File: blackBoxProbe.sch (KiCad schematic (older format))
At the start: 34 parts, among them J1 USB-ID, U1 MCP1702-MB, U2 USBLC6-2, U3 STM32F103CBT

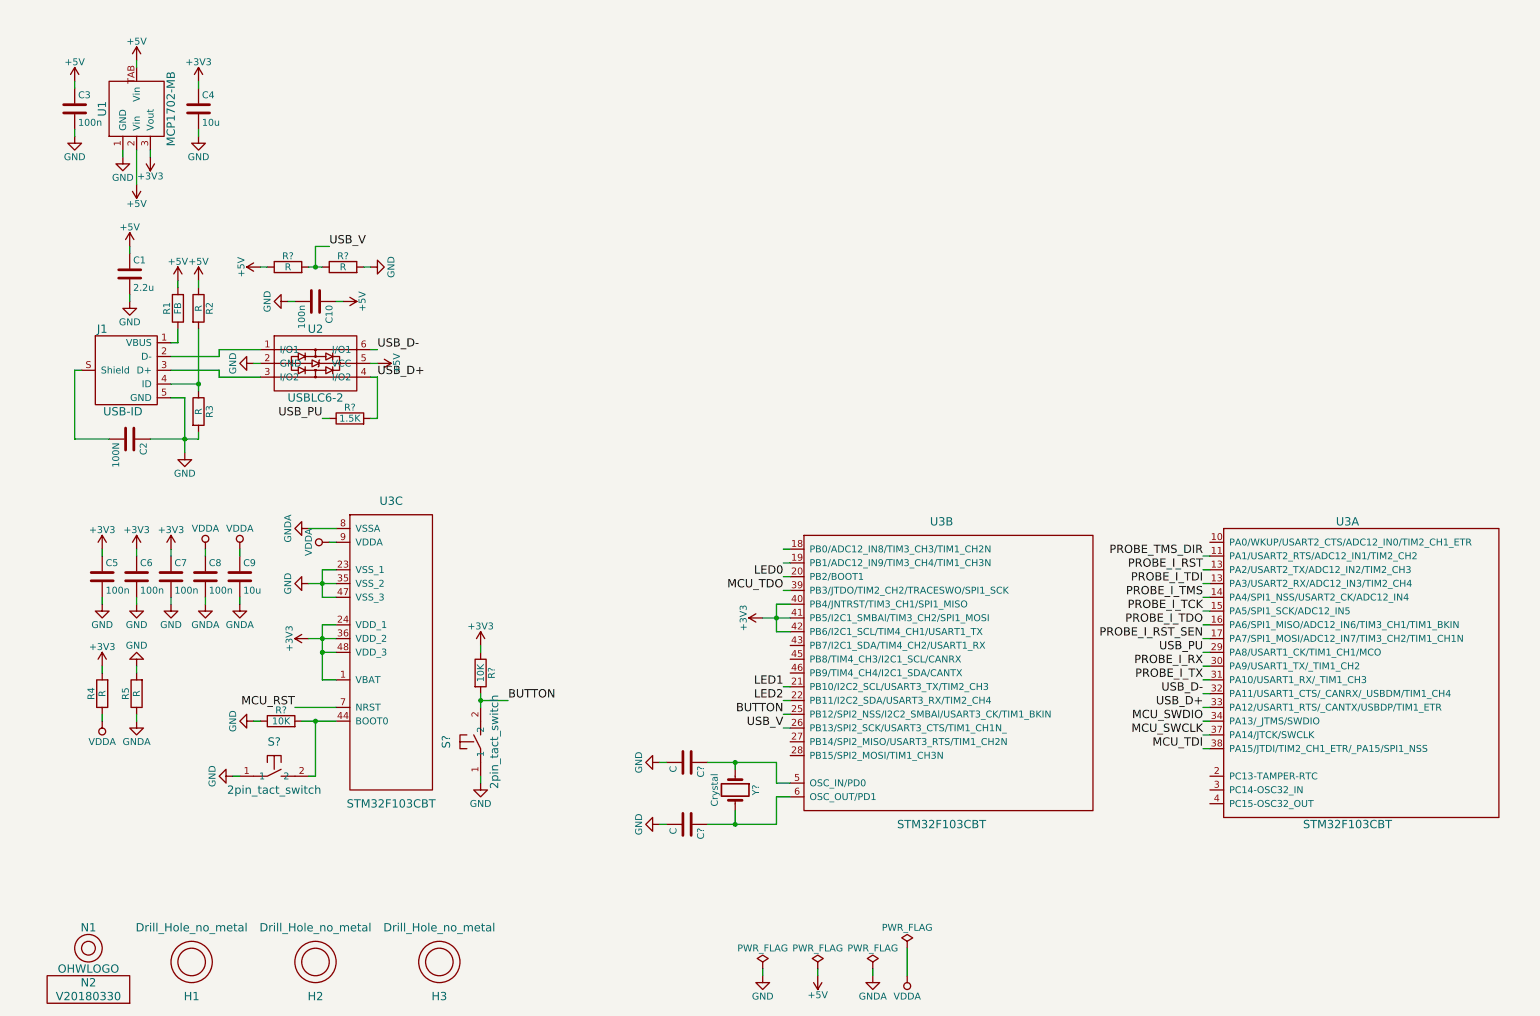
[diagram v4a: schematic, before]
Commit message: WIP: added JTAG/SWD interface bits, still reset sensing needs to be done
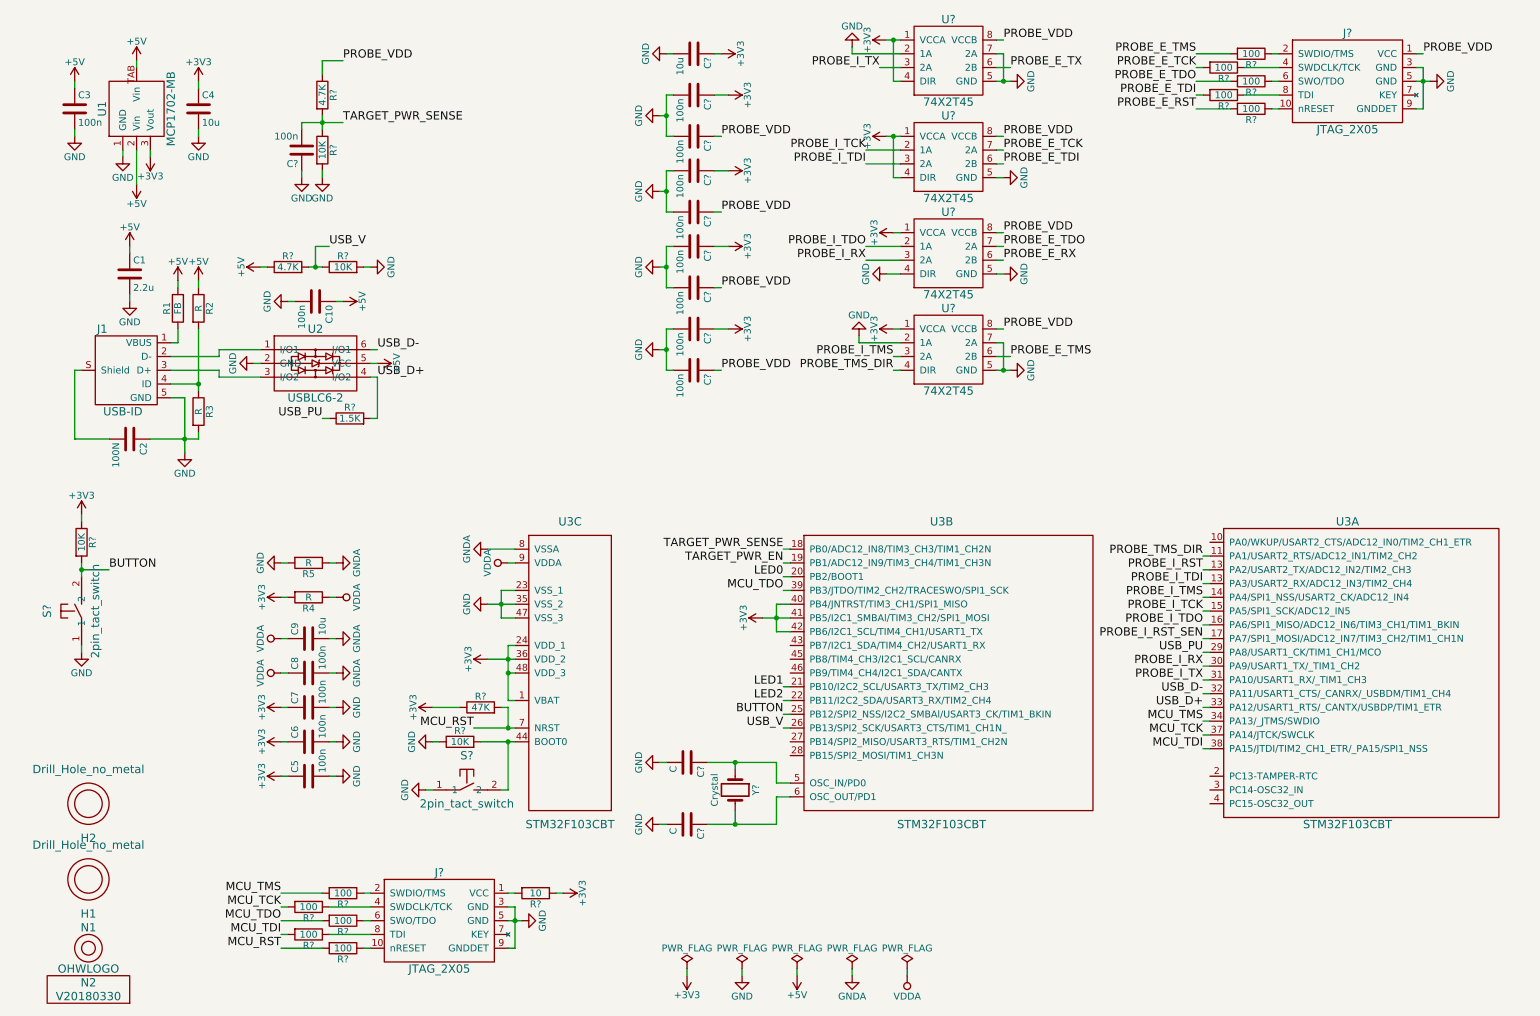
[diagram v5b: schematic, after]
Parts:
- removed H3: Drill_Hole_no_metal, SquantorPcbOutline:MountingHole_2.2mm_no_metal, symbol Drill_Hole_no_metal
- added C? (x9): 100n, SquantorRcl:C_0603, symbol C
- added C?: 10u, SquantorRcl:C_0805, symbol C
- added J? (x2): JTAG_2X05, symbol JTAG_2X05
- added R?: 10K, SquantorRcl:R_0603_hand, symbol R
- added R?: 4.7K, SquantorRcl:R_0603_hand, symbol R
- added R? (x10): 100, SquantorRcl:R_0603_hand, symbol R
- added R?: 10, SquantorRcl:R_0603_hand, symbol R
- added R?: 47K, SquantorRcl:R_0603_hand, symbol R
- added U? (x4): 74X2T45, symbol 74X2T45
- H1, H2: footprint SquantorPcbOutline:MountingHole_3.2mm_no_metal -> SquantorPcbOutline:MountingHole_2.5mm_no_metal
- R?: value R -> 4.7K
- R?: value R -> 10K
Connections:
- net +3V3: now also C?.1, C?.1, C?.1, C?.1, C?.1, R?.1, R?.1, U?.1 (VCCA), U?.1 (VCCA), U?.1 (VCCA), U?.1 (VCCA), U?.4 (DIR), U?.4 (DIR)
- net GND: now also C?.1, C?.2, C?.2, C?.2, C?.2, C?.2, C?.2, C?.2, C?.2, C?.2, J?.3 (GND), J?.3 (GND), J?.5 (GND), J?.5 (GND), J?.9 (GNDDET), J?.9 (GNDDET), R?.2, U?.2 (1A), U?.2 (1A), U?.4 (DIR), U?.5 (GND), U?.5 (GND), U?.5 (GND), U?.5 (GND), U?.7 (2A), U?.7 (2A)
- net MCU_RST: now also R?.2, R?.2
- net MCU_TDI: now also R?.2
- net MCU_TDO: now also R?.2
- net PROBE_I_RX: now also U?.3 (2A)
- net PROBE_I_TCK: now also U?.2 (1A)
- net PROBE_I_TDI: now also U?.3 (2A)
- net PROBE_I_TDO: now also U?.2 (1A)
- net PROBE_I_TMS: now also U?.3 (2A)
- net PROBE_I_TX: now also U?.3 (2A)
- net PROBE_TMS_DIR: now also U?.4 (DIR)
- net TARGET_PWR_SENSE: now reaches U3.18 (PB0/ADC12_IN8/TIM3_CH3/TIM1_CH2N)
- net TARGET_PWR_SENSE: now also C?.2, R?.1, R?.2
- net TARGET_PWR_EN: now reaches U3.19 (PB1/ADC12_IN9/TIM3_CH4/TIM1_CH3N)
- net MCU_SWCLK renamed MCU_TCK
- net MCU_TCK: now also R?.2
- net MCU_SWDIO renamed MCU_TMS
- net MCU_TMS: now also R?.2
- new net: J?.1 (VCC), R?.2
- new net: J?.10 (nRESET), R?.1 (x2)
- new net: J?.2 (SWDIO/TMS), R?.1 (x2)
- new net: J?.4 (SWDCLK/TCK), R?.1 (x2)
- new net: J?.6 (SWO/TDO), R?.1 (x2)
- new net: J?.8 (TDI), R?.1 (x2)
- new net PROBE_E_RST: R?.2
- new net PROBE_E_RX: U?.6 (2B)
- new net PROBE_E_TCK: R?.2, U?.7 (2A)
- new net PROBE_E_TDI: R?.2, U?.6 (2B)
- new net PROBE_E_TDO: R?.2, U?.7 (2A)
- new net PROBE_E_TMS: R?.2, U?.6 (2B)
- new net PROBE_E_TX: U?.6 (2B)
- new net PROBE_VDD: C?.1, C?.1, C?.1, C?.1, J?.1 (VCC), R?.1, U?.8 (VCCB), U?.8 (VCCB), U?.8 (VCCB), U?.8 (VCCB)
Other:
- moved on the sheet: C5, C6, C7, C8, C9, H1, H2, R4, R5, R?, S?, U3C

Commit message: DONE: Finished schematic WIP: review WIP: Assign components
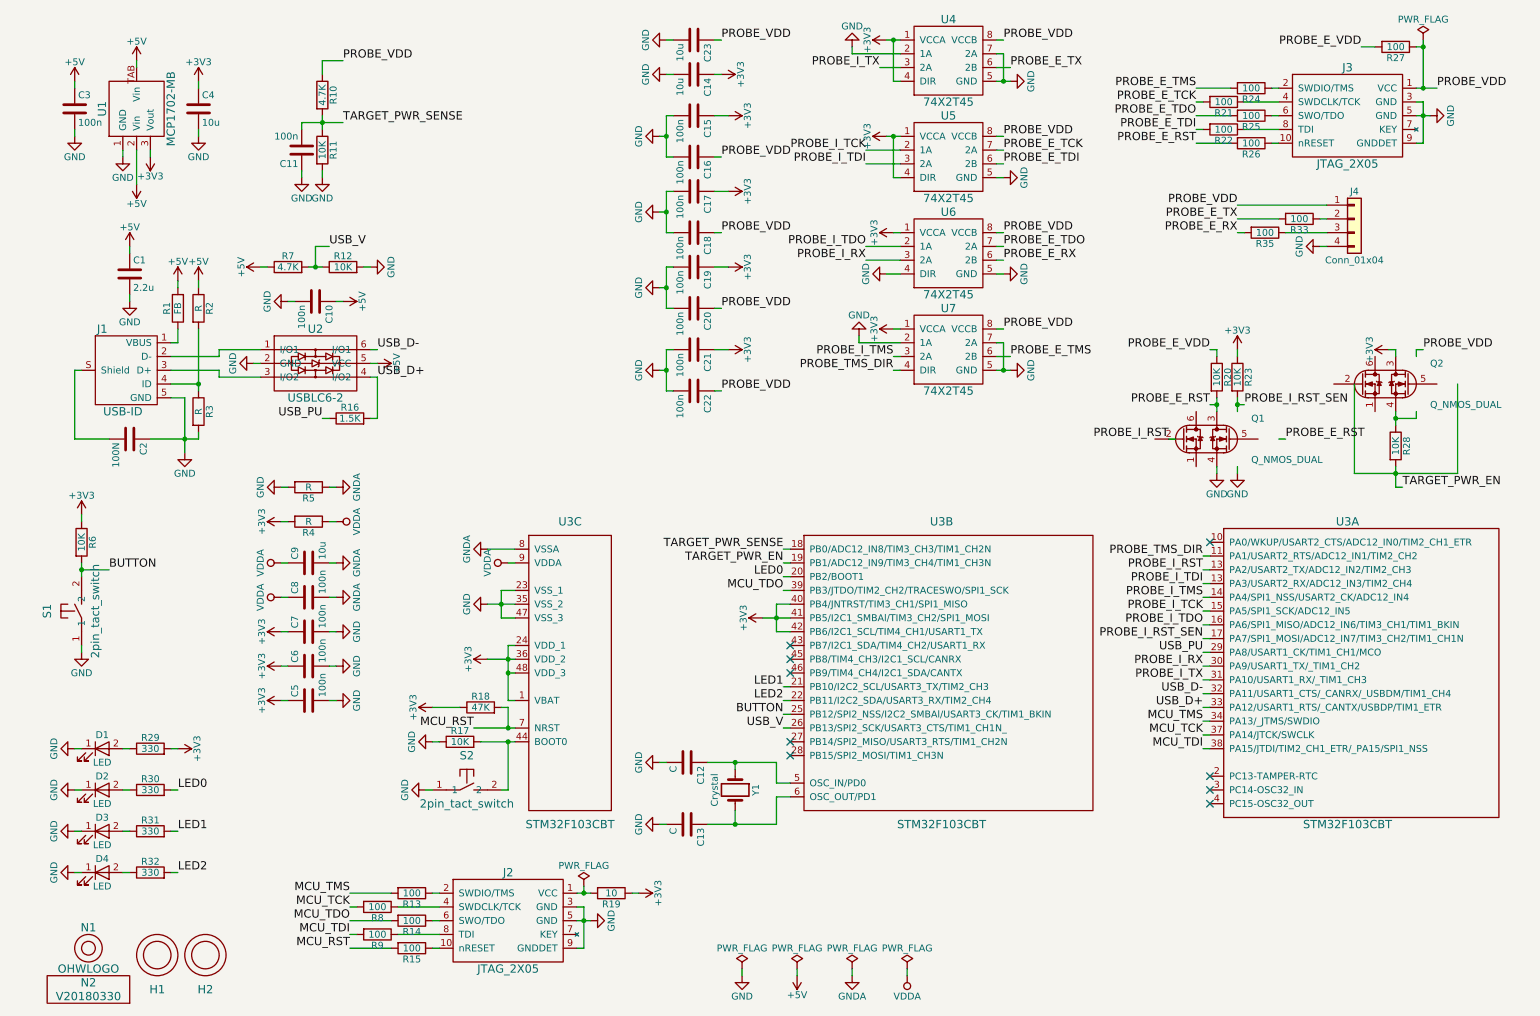
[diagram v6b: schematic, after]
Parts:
- added C23: 10u, SquantorRcl:C_0805, symbol C
- added D1, D2, D3, D4: LED, symbol LED
- added J4: Conn_01x04, symbol Conn_01x04
- added Q1, Q2: Q_NMOS_DUAL, symbol Q_NMOS_DUAL
- added R20, R23, R28: 10K, SquantorRcl:R_0603_hand, symbol R
- added R27, R33, R35: 100, SquantorRcl:R_0603_hand, symbol R
- added R29, R30, R31, R32: 330, SquantorRcl:R_0603_hand, symbol R
- C12, C13: renamed from C?; footprint (none) -> SquantorRcl:C_0603
- J2, J3: renamed from J?; footprint (none) -> SquantorConnectors:Header-0127-2X05-SMD
- U3: footprint SquantorIC:SOT313-2 -> (none)
- U4, U5, U6, U7: renamed from U?; footprint (none) -> SquantorIC:NXP_SOT765-1_HAND
- Y1: renamed from Y?; footprint (none) -> SquantorCrystal:SquantorCrystal-CRYSTAL_5.0X3.2
- gave numbers to parts that had none: 31
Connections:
- net +3V3: now also Q2.3 (D2), R23.1, R29.2
- net GND: now also C23.2, D1.1 (K), D2.1 (K), D3.1 (K), D4.1 (K), J4.4 (Pin_4), Q1.4 (S2)
- net LED0: now also R30.2
- net LED1: now also R31.2
- net LED2: now also R32.2
- net PROBE_E_RST: now also Q1.3 (D2), R20.2
- net PROBE_E_RX: now also R35.2
- net PROBE_E_TX: now also R33.2
- net PROBE_I_RST_SEN: now also R23.2
- net PROBE_VDD: now also C23.1, J4.1 (Pin_1), R27.1
- net TARGET_PWR_EN: now also R28.2
- new net: Q2.4 (S2), R28.1
- new net: D1.2 (A), R29.1
- new net: D2.2 (A), R30.1
- new net: D3.2 (A), R31.1
- new net: D4.2 (A), R32.1
- new net: J4.2 (Pin_2), R33.1
- new net: J4.3 (Pin_3), R35.1
- new net PROBE_E_VDD: R20.1, R27.2
- no-connect marks 0 -> 9
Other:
- moved on the sheet: C14, C15, C16, C17, C18, C19, C20, C21, C22, C5, C6, C7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

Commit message: FIX: fixed wrong schematic symbol for the switch, needs to be dual PMOS DONE: assigned all components a footprint
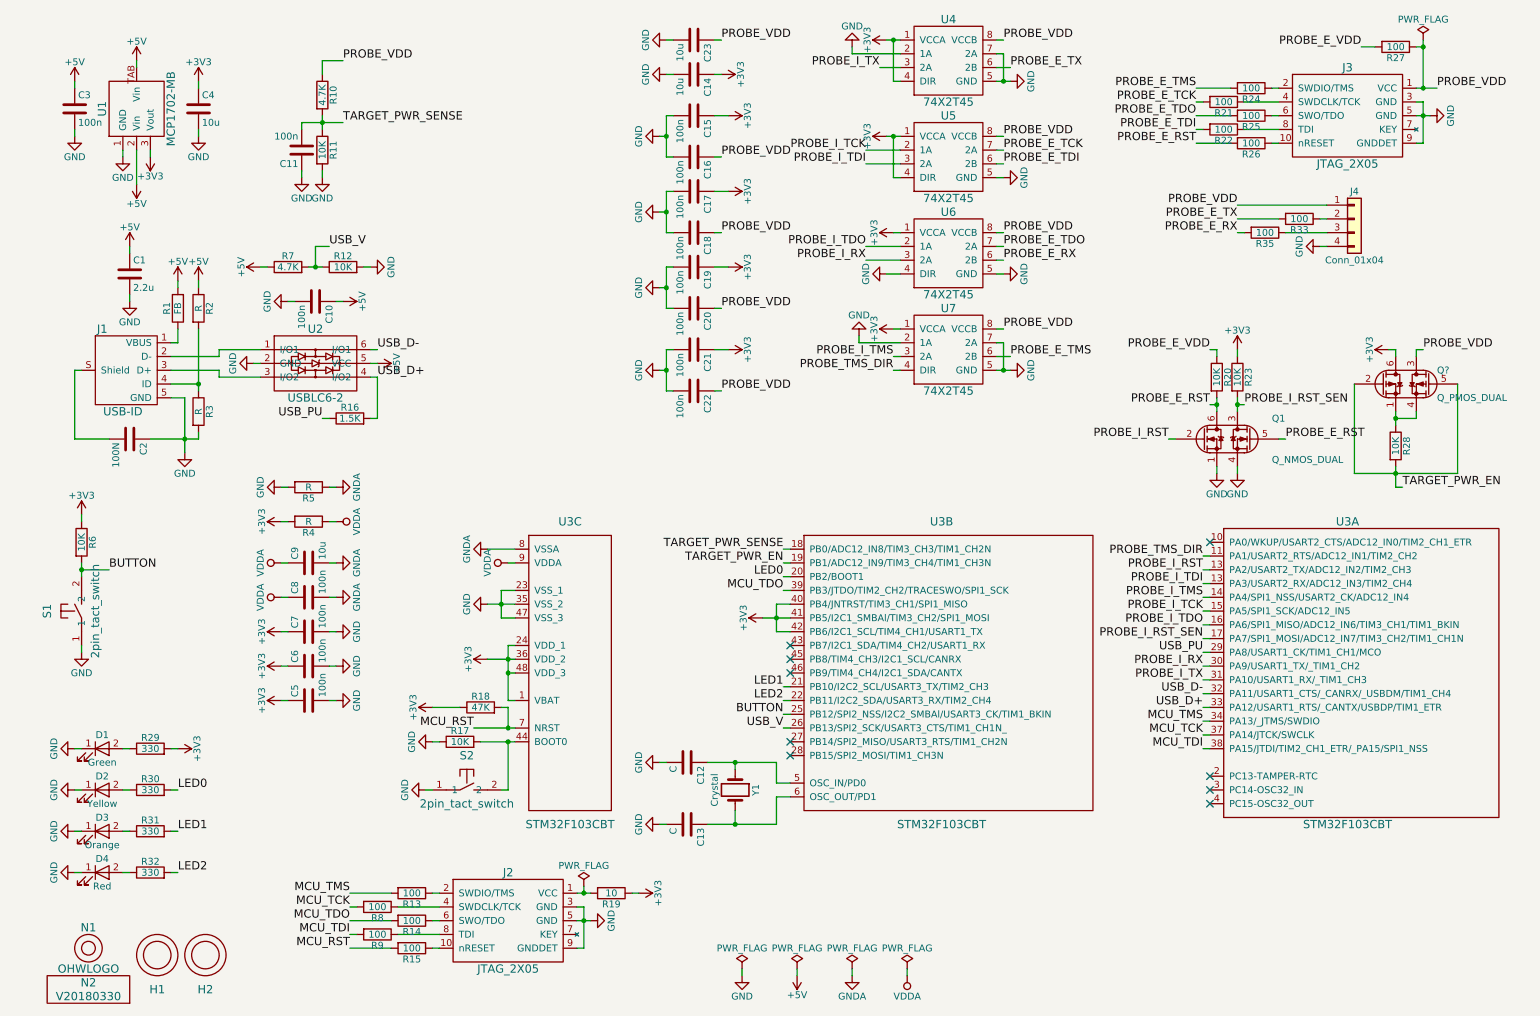
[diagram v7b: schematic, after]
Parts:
- removed Q2: Q_NMOS_DUAL, symbol Q_NMOS_DUAL
- added Q?: Q_PMOS_DUAL, TO_SOT_Packages_SMD:SOT-363_SC-70-6_Handsoldering, symbol Q_PMOS_DUAL
- D1: value LED -> Green; footprint (none) -> LEDs:LED_PLCC-2
- D2: value LED -> Yellow; footprint (none) -> LEDs:LED_PLCC-2
- D3: value LED -> Orange; footprint (none) -> LEDs:LED_PLCC-2
- D4: value LED -> Red; footprint (none) -> LEDs:LED_PLCC-2
- Q1: footprint (none) -> TO_SOT_Packages_SMD:SOT-363_SC-70-6_Handsoldering
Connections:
- net +3V3: now also Q?.6 (D1)
- net GND: now also Q1.1 (S1)
- net PROBE_E_RST: now also Q1.5 (G2), Q1.6 (D1); no longer Q1.3 (D2)
- net PROBE_I_RST: now also Q1.2 (G1)
- net PROBE_I_RST_SEN: now also Q1.3 (D2)
- net PROBE_VDD: now also Q?.3 (D2)
- net TARGET_PWR_EN: now also Q?.2 (G1), Q?.5 (G2)
- net at R28.1: now also Q?.1 (S1), Q?.4 (S2)
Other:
- moved on the sheet: Q1
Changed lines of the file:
@@
 L Q_NMOS_DUAL Q1
 U 1 1 5B245E45
-P 8950 3650
-F 0 "Q1" H 9300 3800 50  0000 L CNN
-F 1 "Q_NMOS_DUAL" H 9300 3500 50  0000 L CNN
-F 2 "" H 9150 3750 50  0001 C CNN
-F 3 "" H 8950 3650 50  0001 C CNN
-	1    8950 3650
+P 9100 3650
+F 0 "Q1" H 9450 3800 50  0000 L CNN
+F 1 "Q_NMOS_DUAL" H 9450 3500 50  0000 L CNN
+F 2 "TO_SOT_Packages_SMD:SOT-363_SC-70-6_Handsoldering" H 9300 3750 50  0001 C CNN
+F 3 "" H 9100 3650 50  0001 C CNN
+	1    9100 3650
 	1    0    0    -1
 $EndComp
@@
 Connection ~ 9200 3400
 $Comp
-L Q_NMOS_DUAL Q2
-U 1 1 5B24D809
-P 10250 3250
-F 0 "Q2" H 10600 3400 50  0000 L CNN
-F 1 "Q_NMOS_DUAL" H 10600 3100 50  0000 L CNN
-F 2 "" H 10450 3350 50  0001 C CNN
-F 3 "" H 10250 3250 50  0001 C CNN
-	1    10250 3250
-	1    0    0    -1
-$EndComp
-$Comp
 L R R28
 U 1 1 5B24DA84
@@
 P 950 5900
 F 0 "D1" H 950 6000 50  0000 C CNN
-F 1 "LED" H 950 5800 50  0000 C CNN
-F 2 "" H 950 5900 50  0001 C CNN
+F 1 "Green" H 950 5800 50  0000 C CNN
+F 2 "LEDs:LED_PLCC-2" H 950 5900 50  0001 C CNN
 F 3 "" H 950 5900 50  0001 C CNN
 	1    950  5900
@@
 P 950 6200
 F 0 "D2" H 950 6300 50  0000 C CNN
-F 1 "LED" H 950 6100 50  0000 C CNN
-F 2 "" H 950 6200 50  0001 C CNN
+F 1 "Yellow" H 950 6100 50  0000 C CNN
+F 2 "LEDs:LED_PLCC-2" H 950 6200 50  0001 C CNN
 F 3 "" H 950 6200 50  0001 C CNN
 	1    950  6200
@@
 P 950 6500
 F 0 "D3" H 950 6600 50  0000 C CNN
-F 1 "LED" H 950 6400 50  0000 C CNN
-F 2 "" H 950 6500 50  0001 C CNN
+F 1 "Orange" H 950 6400 50  0000 C CNN
+F 2 "LEDs:LED_PLCC-2" H 950 6500 50  0001 C CNN
 F 3 "" H 950 6500 50  0001 C CNN
 	1    950  6500
@@
 P 950 6800
 F 0 "D4" H 950 6900 50  0000 C CNN
-F 1 "LED" H 950 6700 50  0000 C CNN
-F 2 "" H 950 6800 50  0001 C CNN
+F 1 "Red" H 950 6700 50  0000 C CNN
+F 2 "LEDs:LED_PLCC-2" H 950 6800 50  0001 C CNN
 F 3 "" H 950 6800 50  0001 C CNN
 	1    950  6800
@@
 $EndComp
 Connection ~ 10550 800
+$Comp
+L Q_PMOS_DUAL Q?
+U 1 1 5B2C36DB
+P 10400 3250
+F 0 "Q?" H 10650 3350 50  0000 L CNN
+F 1 "Q_PMOS_DUAL" H 10650 3150 50  0000 L CNN
+F 2 "TO_SOT_Packages_SMD:SOT-363_SC-70-6_Handsoldering" H 10450 3350 50  0001 C CNN
+F 3 "" H 10250 3250 50  0001 C CNN
+	1    10400 3250
+	1    0    0    -1
+$EndComp
 $EndSCHEMATC
